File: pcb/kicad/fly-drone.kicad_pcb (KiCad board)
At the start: 2 copper layers, 83.2 x 83.2 mm, 33 parts, among them M1 8520 motor, M2 8520 motor, M3 8520 motor, M4 8520 motor, Q1 IRLB8721, Q2 IRLB8721, Q3 IRLB8721, Q4 IRLB8721, U2 GY-521 MPU6050

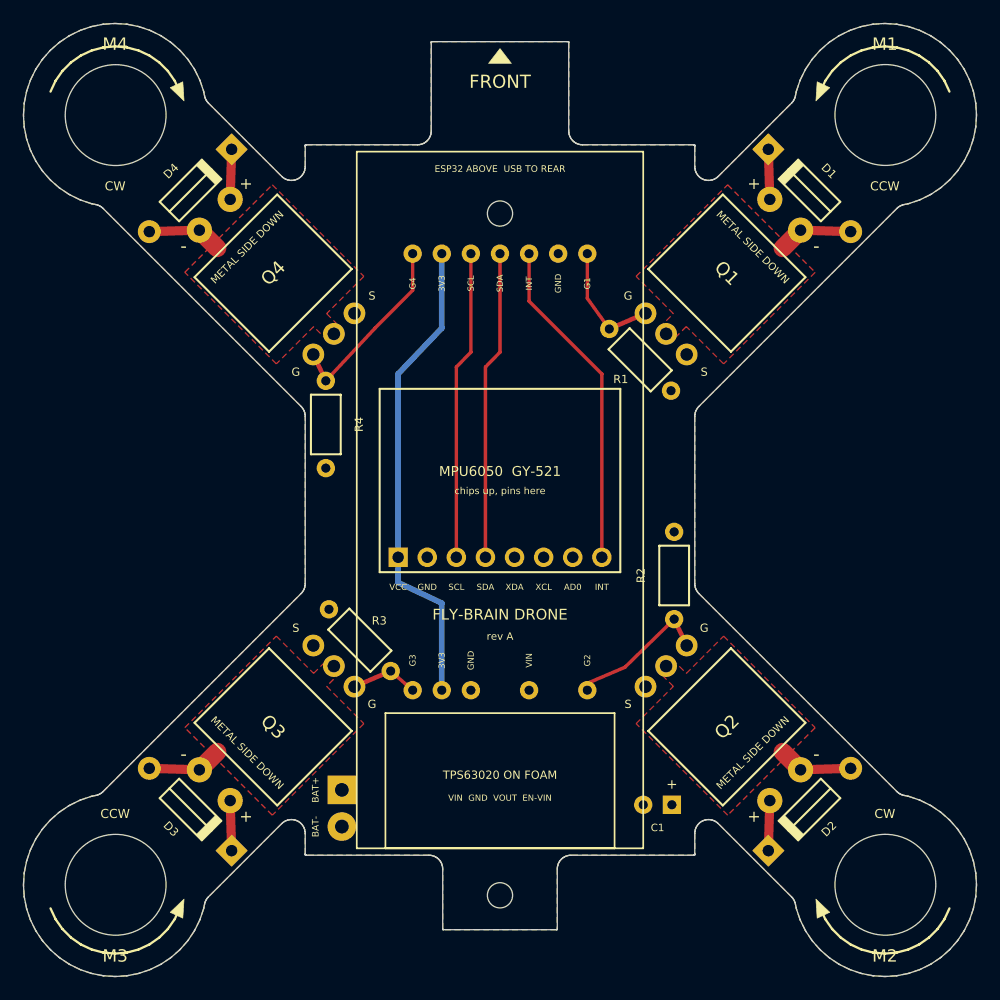
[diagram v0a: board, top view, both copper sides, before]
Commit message: Make the silkscreen readable for fabrication
All labels are now at least 0.85 mm tall (JLCPCB's minimum is 0.8 mm),
motor names no longer sit on their spin arrows, and long labels are
shortened. KiCad 10 DRC: 0 errors, 0 unconnected items. Copper, drills
and outline are unchanged. Adds KiCad 3D renders of both sides.

Co-Authored-By: Claude Opus 5.5 <noreply@anthropic.com>
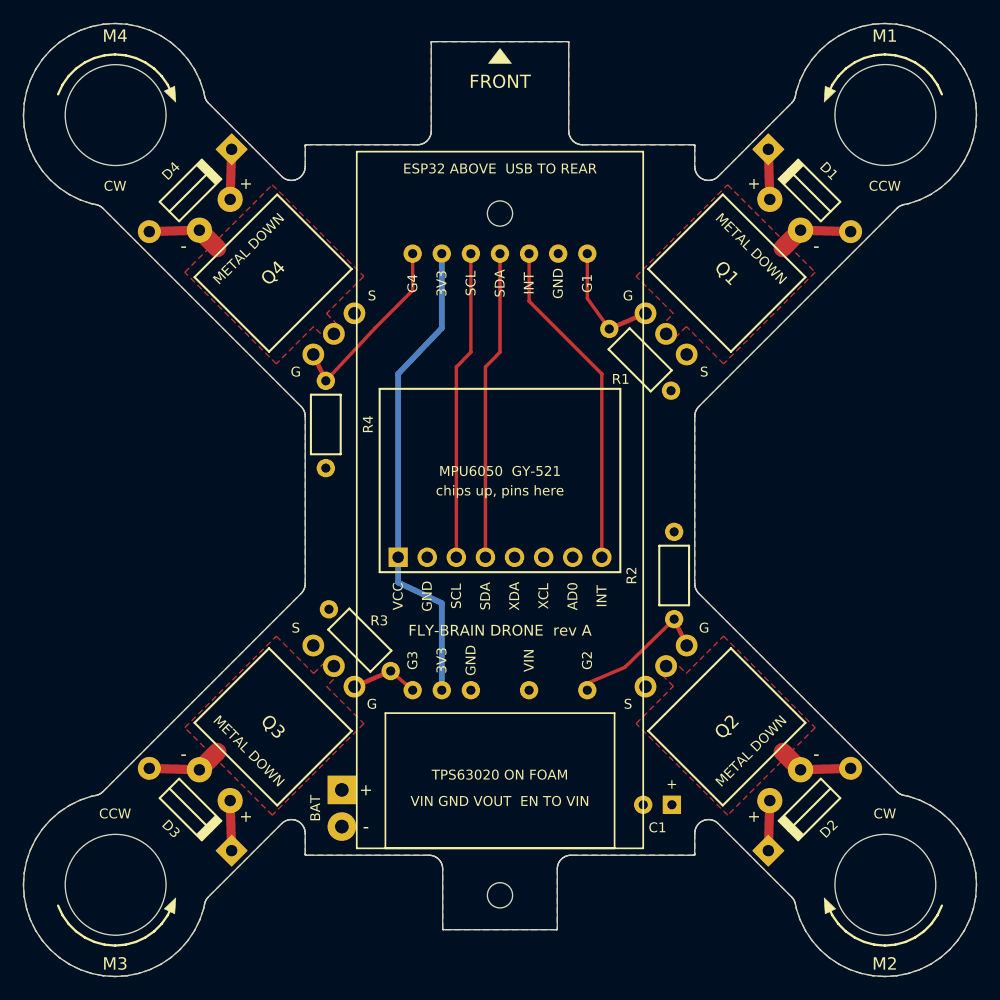
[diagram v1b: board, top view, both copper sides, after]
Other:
- board text added: "BAT"
- board text added: "FLY-BRAIN DRONE rev A"
- board text added: "METAL DOWN"
- board text added: "VIN GND VOUT EN TO VIN"
- board text removed: "BAT+"
- board text removed: "BAT-"
- board text removed: "FLY-BRAIN DRONE"
- board text removed: "METAL SIDE DOWN"
- board text removed: "VIN GND VOUT EN-VIN"
- board text removed: "rev A"
